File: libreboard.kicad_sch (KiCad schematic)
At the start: 70 parts, among them J100 Screw Terminal, J101 Screw Terminal, J11 USB_C_Receptacle_USB2.0, J51 12V Fan 1, J52 12V Fan 2, J53 12V Fan 3, J54 12V Fan 4, U10 EMC2305-x-AP, U14 PTPS55289RYQR, U4 PTPS55289RYQR

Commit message: fix all DRC issues
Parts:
- U14, U4: footprint libreboard:RYQ0021A-MFG -> RYQ0021A-MFG
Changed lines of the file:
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@@
 			)
 		)
-		(property "Footprint" "libreboard:RYQ0021A-MFG"
+		(property "Footprint" "RYQ0021A-MFG"
 			(at 173.99 194.31 0)
 			(effects
@@
 			)
 		)
-		(property "Datasheet" "https://www.ti.com/lit/ds/symlink/tps55289.pdf"
+		(property "Datasheet" "PTPS55289RYQR"
 			(at 173.99 194.31 0)
 			(effects
@@
 	)
 	(symbol
+		(lib_name "PTPS55289RYQR_1")
 		(lib_id "TPS55289:PTPS55289RYQR")
 		(at 177.8 306.07 0)
@@
 			)
 		)
-		(property "Footprint" "libreboard:RYQ0021A-MFG"
+		(property "Footprint" "RYQ0021A-MFG"
 			(at 177.8 306.07 0)
 			(effects
@@
 			)
 		)
-		(property "Datasheet" "https://www.ti.com/lit/ds/symlink/tps55289.pdf"
+		(property "Datasheet" "PTPS55289RYQR"
 			(at 177.8 306.07 0)
 			(effects

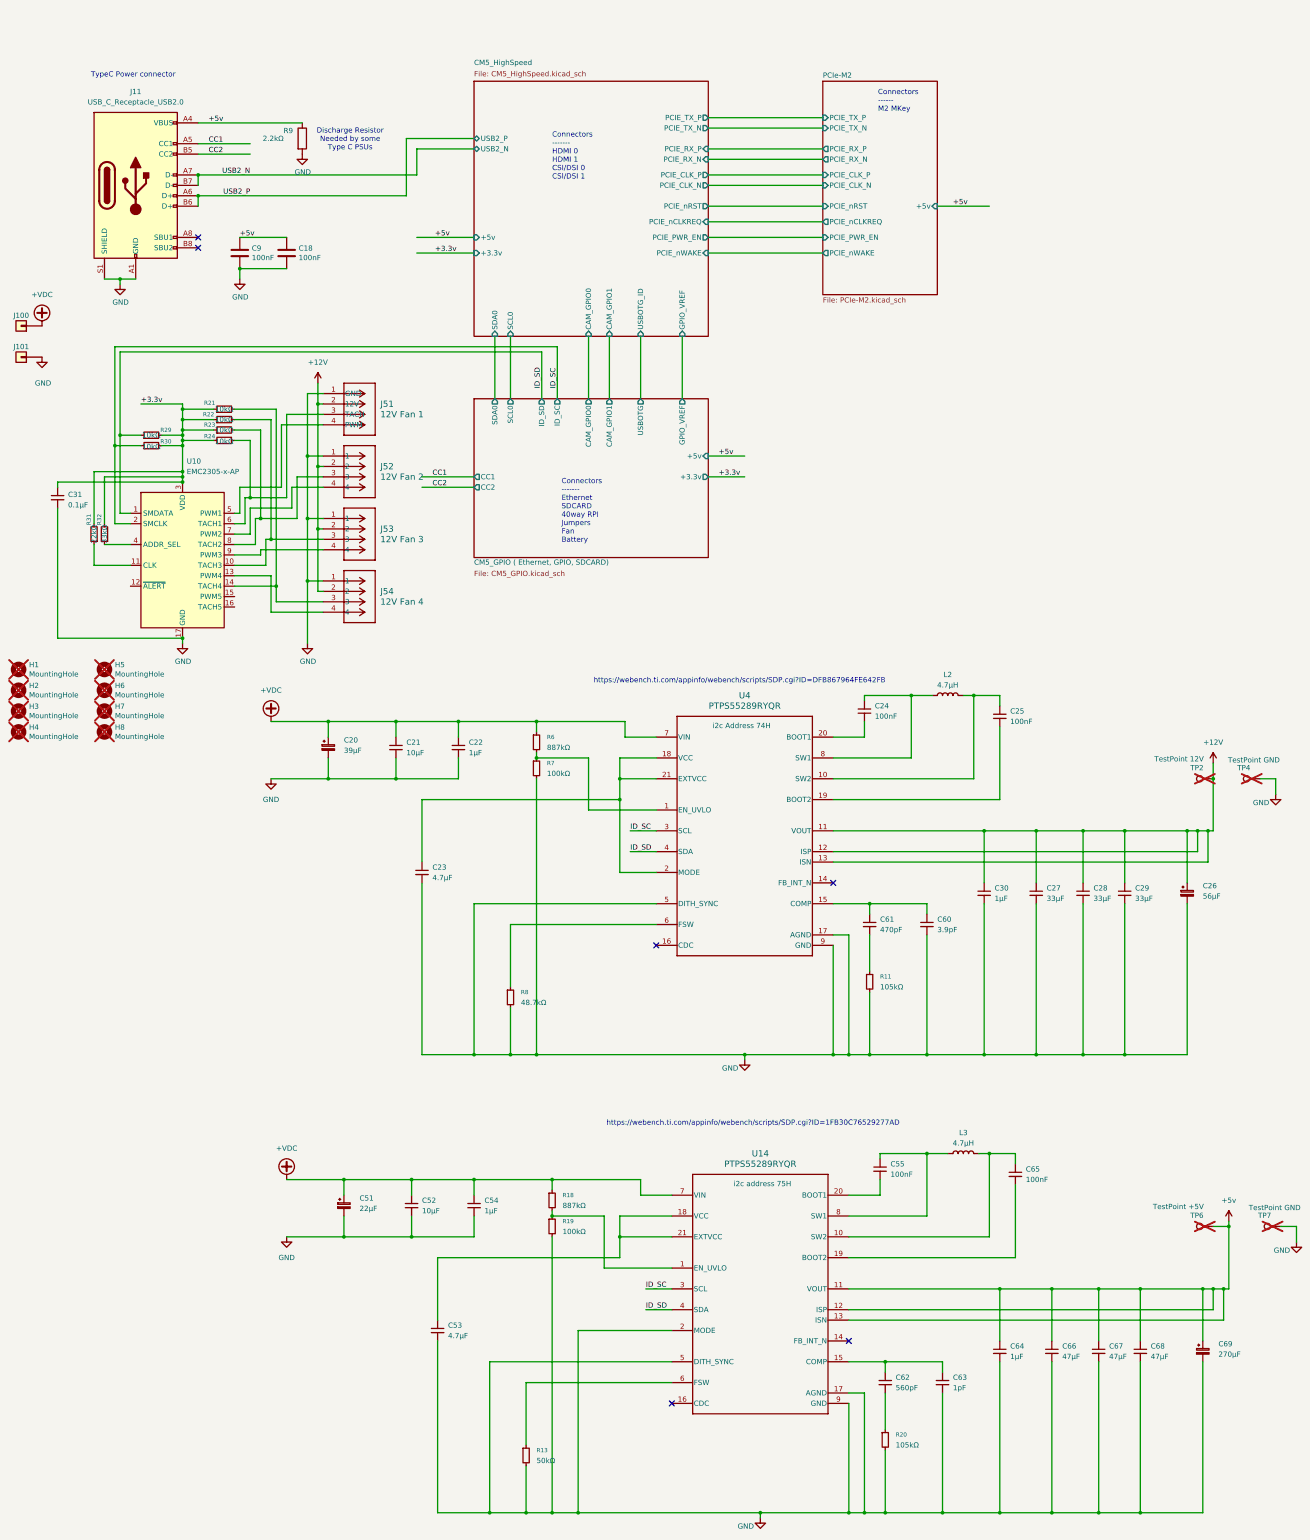
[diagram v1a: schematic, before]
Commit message: final review, added coincell back, additional testpoints, updated i2c bus for quic
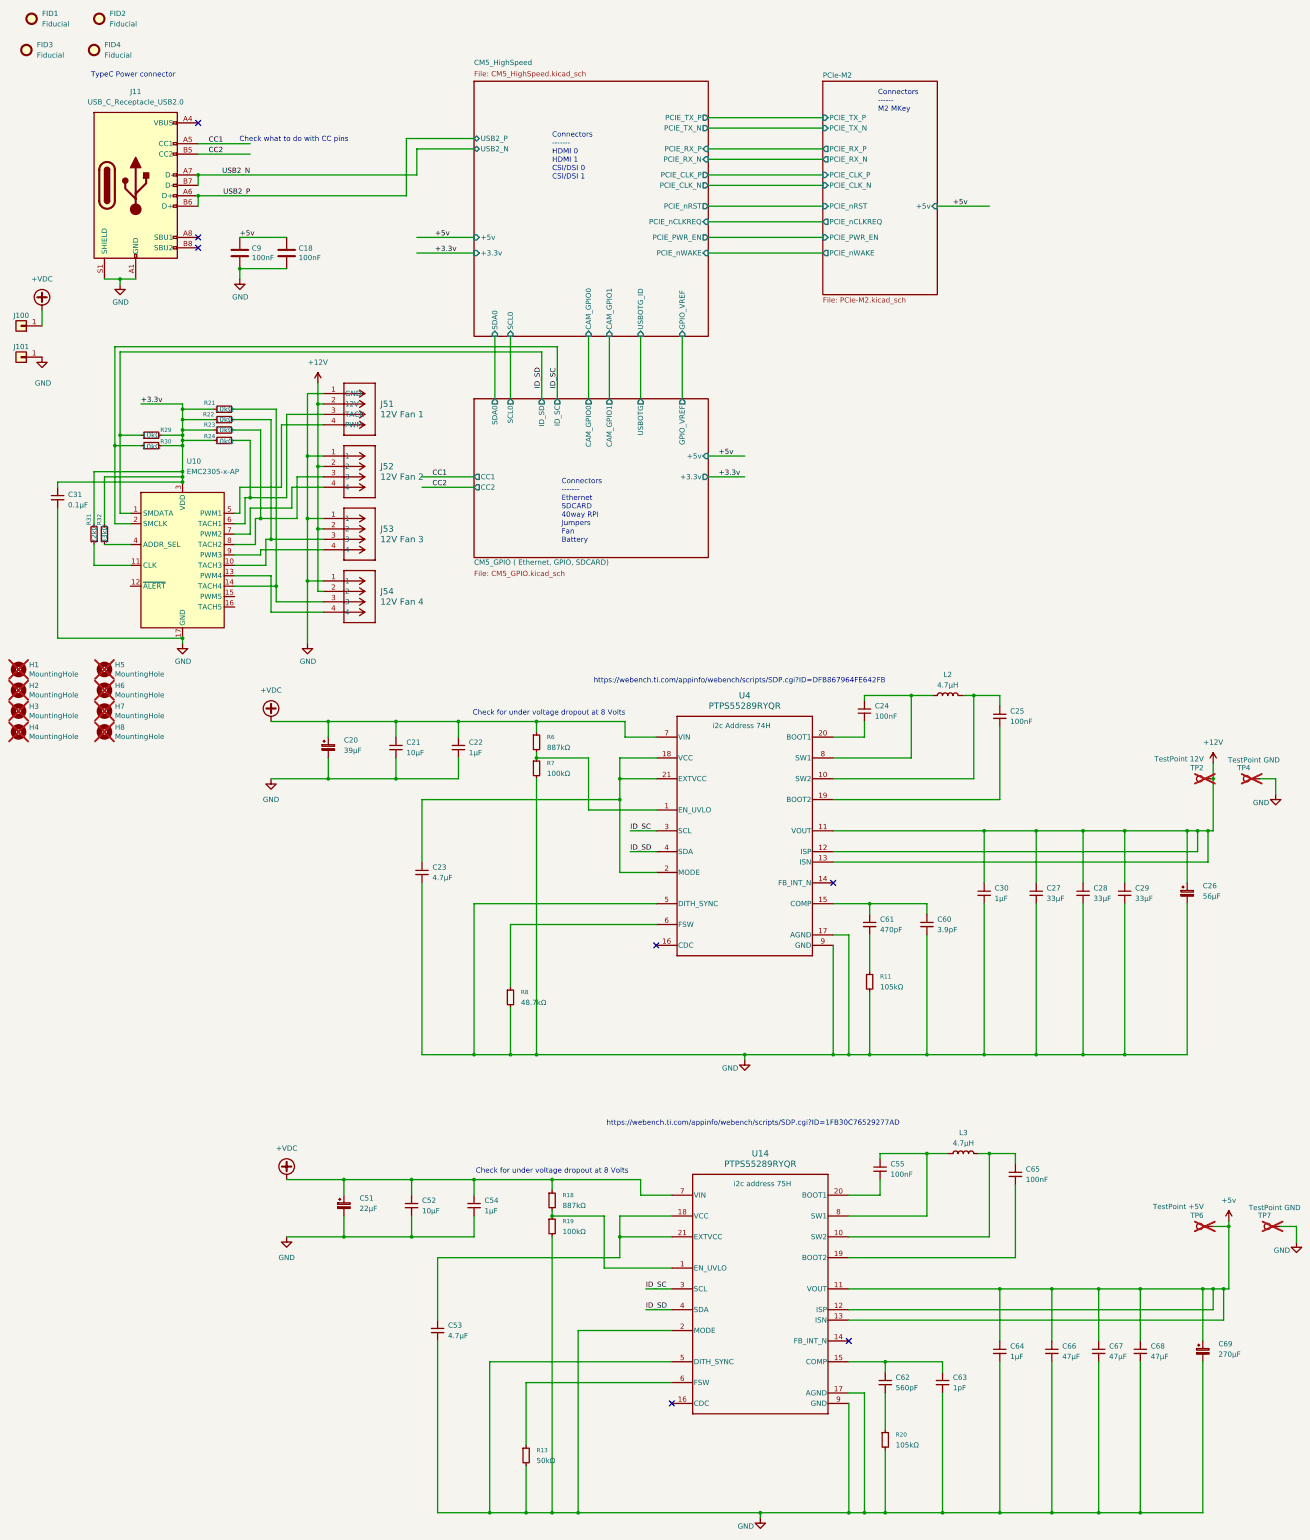
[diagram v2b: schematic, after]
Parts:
- removed R9: 2.2kΩ, Resistor_SMD:R_0402_1005Metric, symbol Device:R
- added FID1, FID2, FID3, FID4: Fiducial, Fiducial:Fiducial_1mm_Mask2mm, symbol Mechanical:Fiducial
- J11: footprint Connector_USB:USB_C_Receptacle_GCT_USB4105-GF-A_16P_TopMnt_Horizontal -> libreboard:USB_C_Receptacle_GCT_USB4105-xx-A_16P_TopMnt_Horizontal
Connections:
- net +5v: no longer J11.A4 (VBUS), J11.A9 (VBUS), J11.B4 (VBUS), J11.B9 (VBUS)
- new net: J11.A4 (VBUS), J11.A9 (VBUS), J11.B4 (VBUS), J11.B9 (VBUS)
- no-connect marks 6 -> 7
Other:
- note added: "Check for under voltage dropout at 8 Volts"
- note added: "Check what to do with CC pins"
- note removed: "Discharge Resistor Needed by some Type C PSUs"

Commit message: Rev1
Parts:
- C22, C54: Dist. P/N 478-KGM05AR50J105KHTR-ND -> 490-GRM155R61H105KE05DTR-ND; Manf. P/N 04026D105KAT2A -> GRM155R61H105KE05D; Manufacturer Kyocera -> Murata Electronics; Part Description Capacitor, Ceramic, 1µF, ±10%, 6.3V, X5R, 0402 (1005m) -> 1 µF ±10% 50V Ceramic Capacitor X5R 0402 (1005 Metric)
- C24, C25, C55, C65: Dist. P/N 478-11504-2-ND -> 490-10700-2-ND; Manf. P/N 04026D104KAT4A -> GRM155R71H104KE14D; Manufacturer Kyocera -> Murata Electronics; Part Description Capacitor, Ceramic, 0.1µF, ±10%, 6.3V, X5R, 0402 (1005m) -> CAP CER 0.1UF 50V X7R 0402
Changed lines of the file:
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@@
 			)
 		)
-		(property "Dist. P/N" "478-KGM05AR50J105KHTR-ND"
+		(property "Dist. P/N" "490-GRM155R61H105KE05DTR-ND"
 			(at 125.73 196.85 0)
 			(effects
@@
 			)
 		)
-		(property "Manf. P/N" "04026D105KAT2A"
+		(property "Manf. P/N" "GRM155R61H105KE05D"
 			(at 125.73 196.85 0)
 			(effects
@@
 			)
 		)
-		(property "Manufacturer" "Kyocera"
+		(property "Manufacturer" "Murata Electronics"
 			(at 125.73 196.85 0)
 			(effects
@@
 			)
 		)
-		(property "Part Description" "Capacitor, Ceramic, 1µF, ±10%, 6.3V, X5R, 0402 (1005m)"
+		(property "Part Description" "1 µF ±10% 50V Ceramic Capacitor X5R 0402 (1005 Metric)"
 			(at 125.73 196.85 0)
 			(effects
@@
 			)
 		)
-		(property "Dist. P/N" "478-KGM05AR50J105KHTR-ND"
+		(property "Dist. P/N" "490-GRM155R61H105KE05DTR-ND"
 			(at 129.54 308.61 0)
 			(effects
@@
 			)
 		)
-		(property "Manf. P/N" "04026D105KAT2A"
+		(property "Manf. P/N" "GRM155R61H105KE05D"
 			(at 129.54 308.61 0)
 			(effects
@@
 			)
 		)
-		(property "Manufacturer" "Kyocera"
+		(property "Manufacturer" "Murata Electronics"
 			(at 129.54 308.61 0)
 			(effects
@@
 			)
 		)
-		(property "Part Description" "Capacitor, Ceramic, 1µF, ±10%, 6.3V, X5R, 0402 (1005m)"
+		(property "Part Description" "1 µF ±10% 50V Ceramic Capacitor X5R 0402 (1005 Metric)"
 			(at 129.54 308.61 0)
 			(effects
@@
 			)
 		)
-		(property "Datasheet" "~"
+		(property "Datasheet" "https://search.murata.co.jp/Ceramy/image/img/A01X/G101/ENG/GRM155R71H104KE14-01.pdf"
 			(at 257.81 189.23 0)
 			(effects
@@
 			)
 		)
-		(property "Dist. P/N" "478-11504-2-ND"
+		(property "Dist. P/N" "490-10700-2-ND"
 			(at 257.81 189.23 0)
 			(effects
@@
 			)
 		)
-		(property "Manf. P/N" "04026D104KAT4A"
+		(property "Manf. P/N" "GRM155R71H104KE14D"
 			(at 257.81 189.23 0)
 			(effects
@@
 			)
 		)
-		(property "Manufacturer" "Kyocera"
+		(property "Manufacturer" "Murata Electronics"
 			(at 257.81 189.23 0)
 			(effects
@@
 			)
 		)
-		(property "Part Description" "Capacitor, Ceramic, 0.1µF, ±10%, 6.3V, X5R, 0402 (1005m)"
+		(property "Part Description" "CAP CER 0.1UF 50V X7R 0402"
 			(at 257.81 189.23 0)
 			(effects
@@
 			)
 		)
-		(property "Datasheet" "~"
+		(property "Datasheet" "https://search.murata.co.jp/Ceramy/image/img/A01X/G101/ENG/GRM155R71H104KE14-01.pdf"
 			(at 228.6 299.72 0)
 			(effects
@@
 			)
 		)
-		(property "Dist. P/N" "478-11504-2-ND"
+		(property "Dist. P/N" "490-10700-2-ND"
 			(at 228.6 299.72 0)
 			(effects
@@
 			)
 		)
-		(property "Manf. P/N" "04026D104KAT4A"
+		(property "Manf. P/N" "GRM155R71H104KE14D"
 			(at 228.6 299.72 0)
 			(effects
@@
 			)
 		)
-		(property "Manufacturer" "Kyocera"
+		(property "Manufacturer" "Murata Electronics"
 			(at 228.6 299.72 0)
 			(effects
@@
 			)
 		)
-		(property "Part Description" "Capacitor, Ceramic, 0.1µF, ±10%, 6.3V, X5R, 0402 (1005m)"
+		(property "Part Description" "CAP CER 0.1UF 50V X7R 0402"
 			(at 228.6 299.72 0)
 			(effects
@@
 			)
 		)
-		(property "Datasheet" "~"
+		(property "Datasheet" "https://search.murata.co.jp/Ceramy/image/img/A01X/G101/ENG/GRM155R71H104KE14-01.pdf"
 			(at 261.62 300.99 0)
 			(effects
@@
 			)
 		)
-		(property "Dist. P/N" "478-11504-2-ND"
+		(property "Dist. P/N" "490-10700-2-ND"
 			(at 261.62 300.99 0)
 			(effects
@@
 			)
 		)
-		(property "Manf. P/N" "04026D104KAT4A"
+		(property "Manf. P/N" "GRM155R71H104KE14D"
 			(at 261.62 300.99 0)
 			(effects
@@
 			)
 		)
-		(property "Manufacturer" "Kyocera"
+		(property "Manufacturer" "Murata Electronics"
 			(at 261.62 300.99 0)
 			(effects
@@
 			)
 		)
-		(property "Part Description" "Capacitor, Ceramic, 0.1µF, ±10%, 6.3V, X5R, 0402 (1005m)"
+		(property "Part Description" "CAP CER 0.1UF 50V X7R 0402"
 			(at 261.62 300.99 0)
 			(effects
@@
 			)
 		)
-		(property "Datasheet" "~"
+		(property "Datasheet" "https://search.murata.co.jp/Ceramy/image/img/A01X/G101/ENG/GRM155R71H104KE14-01.pdf"
 			(at 224.79 187.96 0)
 			(effects
@@
 			)
 		)
-		(property "Dist. P/N" "478-11504-2-ND"
+		(property "Dist. P/N" "490-10700-2-ND"
 			(at 224.79 187.96 0)
 			(effects
@@
 			)
 		)
-		(property "Manf. P/N" "04026D104KAT4A"
+		(property "Manf. P/N" "GRM155R71H104KE14D"
 			(at 224.79 187.96 0)
 			(effects
@@
 			)
 		)
-		(property "Manufacturer" "Kyocera"
+		(property "Manufacturer" "Murata Electronics"
 			(at 224.79 187.96 0)
 			(effects
@@
 			)
 		)
-		(property "Part Description" "Capacitor, Ceramic, 0.1µF, ±10%, 6.3V, X5R, 0402 (1005m)"
+		(property "Part Description" "CAP CER 0.1UF 50V X7R 0402"
 			(at 224.79 187.96 0)
 			(effects

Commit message: switch C21 and C52 to 50V, 0805 size and reposition; Rev2 text
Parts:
- C21, C52: footprint Capacitor_SMD:C_0402_1005Metric -> Capacitor_SMD:C_0805_2012Metric; Dist. P/N 478-KGM05CR50J106MHTR-ND -> 490-18663-2-ND; Manf. P/N 04026D106MAT2A -> GRM21BR61H106KE43L; Manufacturer Kyocera -> Murata Electronics; Part Description Capacitor, Ceramic, 10µF, ±20%, 6.3V, X5R, 0402 (1005m) -> 10 µF ±10% 50V Ceramic Capacitor X5R 0805 (2012 Metric)
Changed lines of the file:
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@@
 			)
 		)
-		(property "Footprint" "Capacitor_SMD:C_0402_1005Metric"
+		(property "Footprint" "Capacitor_SMD:C_0805_2012Metric"
 			(at 114.3 308.61 0)
 			(effects
@@
 			)
 		)
-		(property "Datasheet" "~"
+		(property "Datasheet" "https://search.murata.co.jp/Ceramy/image/img/A01X/G101/ENG/GRM21BR61H106KE43-01A.pdf"
 			(at 114.3 308.61 0)
 			(effects
@@
 			)
 		)
-		(property "Dist. P/N" "478-KGM05CR50J106MHTR-ND"
+		(property "Dist. P/N" "490-18663-2-ND"
 			(at 114.3 308.61 0)
 			(effects
@@
 			)
 		)
-		(property "Manf. P/N" "04026D106MAT2A"
+		(property "Manf. P/N" "GRM21BR61H106KE43L"
 			(at 114.3 308.61 0)
 			(effects
@@
 			)
 		)
-		(property "Manufacturer" "Kyocera"
+		(property "Manufacturer" "Murata Electronics"
 			(at 114.3 308.61 0)
 			(effects
@@
 			)
 		)
-		(property "Part Description" "Capacitor, Ceramic, 10µF, ±20%, 6.3V, X5R, 0402 (1005m)"
+		(property "Part Description" "10 µF ±10% 50V Ceramic Capacitor X5R 0805 (2012 Metric)"
 			(at 114.3 308.61 0)
 			(effects
@@
 			)
 		)
-		(property "Footprint" "Capacitor_SMD:C_0402_1005Metric"
+		(property "Footprint" "Capacitor_SMD:C_0805_2012Metric"
 			(at 110.49 196.85 0)
 			(effects
@@
 			)
 		)
-		(property "Datasheet" "~"
+		(property "Datasheet" "https://search.murata.co.jp/Ceramy/image/img/A01X/G101/ENG/GRM21BR61H106KE43-01A.pdf"
 			(at 110.49 196.85 0)
 			(effects
@@
 			)
 		)
-		(property "Dist. P/N" "478-KGM05CR50J106MHTR-ND"
+		(property "Dist. P/N" "490-18663-2-ND"
 			(at 110.49 196.85 0)
 			(effects
@@
 			)
 		)
-		(property "Manf. P/N" "04026D106MAT2A"
+		(property "Manf. P/N" "GRM21BR61H106KE43L"
 			(at 110.49 196.85 0)
 			(effects
@@
 			)
 		)
-		(property "Manufacturer" "Kyocera"
+		(property "Manufacturer" "Murata Electronics"
 			(at 110.49 196.85 0)
 			(effects
@@
 			)
 		)
-		(property "Part Description" "Capacitor, Ceramic, 10µF, ±20%, 6.3V, X5R, 0402 (1005m)"
+		(property "Part Description" "10 µF ±10% 50V Ceramic Capacitor X5R 0805 (2012 Metric)"
 			(at 110.49 196.85 0)
 			(effects
